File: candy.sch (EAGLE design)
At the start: 8 parts

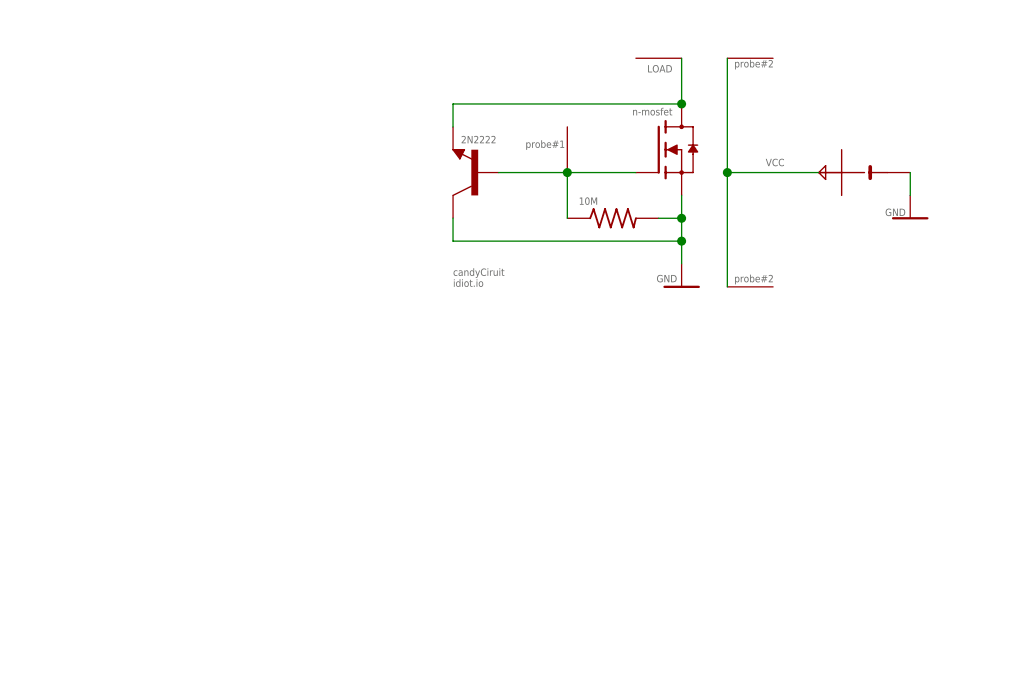
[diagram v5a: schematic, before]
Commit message: removed frame
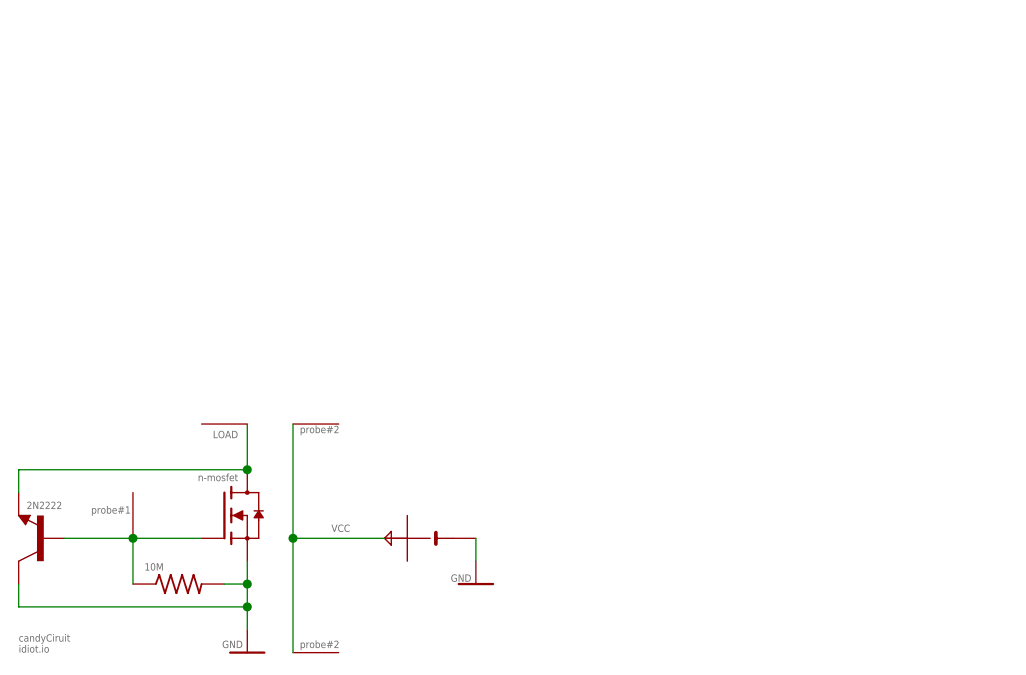
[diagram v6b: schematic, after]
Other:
- moved on the sheet: 10M, 2N2222

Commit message: stick on front
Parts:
- removed 2N2222: (no value), TinyTony_ShenzenReady:2N2222-NPN-TO92-EBC
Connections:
- net GND: no longer 2N2222.C
- net LOAD: no longer 2N2222.E
- net N$1: no longer 2N2222.B
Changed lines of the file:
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@@
 <?xml version="1.0" encoding="utf-8"?>
 <!DOCTYPE eagle SYSTEM "eagle.dtd">
-<eagle version="8.7.0">
+<eagle version="9.0.1">
 <drawing>
 <settings>
@@
 <grid distance="0.1" unitdist="inch" unit="inch" style="lines" multiple="1" display="no" altdistance="0.01" altunitdist="inch" altunit="inch"/>
 <layers>
-<layer number="1" name="Top" color="4" fill="1" visible="no" active="no"/>
-<layer number="16" name="Bottom" color="1" fill="1" visible="no" active="no"/>
-<layer number="17" name="Pads" color="2" fill="1" visible="no" active="no"/>
-<layer number="18" name="Vias" color="2" fill="1" visible="no" active="no"/>
-<layer number="19" name="Unrouted" color="6" fill="1" visible="no" active="no"/>
-<layer number="20" name="Dimension" color="24" fill="1" visible="no" active="no"/>
-<layer number="21" name="tPlace" color="7" fill="1" visible="no" active="no"/>
-<layer number="22" name="bPlace" color="7" fill="1" visible="no" active="no"/>
-<layer number="23" name="tOrigins" color="15" fill="1" visible="no" active="no"/>
-<layer number="24" name="bOrigins" color="15" fill="1" visible="no" active="no"/>
-<layer number="25" name="tNames" color="7" fill="1" visible="no" active="no"/>
-<layer number="26" name="bNames" color="7" fill="1" visible="no" active="no"/>
-<layer number="27" name="tValues" color="7" fill="1" visible="no" active="no"/>
-<layer number="28" name="bValues" color="7" fill="1" visible="no" active="no"/>
+<layer number="1" name="Top" color="4" fill="1" visible="yes" active="no"/>
+<layer number="16" name="Bottom" color="1" fill="1" visible="yes" active="no"/>
+<layer number="17" name="Pads" color="2" fill="1" visible="yes" active="no"/>
+<layer number="18" name="Vias" color="2" fill="1" visible="yes" active="no"/>
+<layer number="19" name="Unrouted" color="6" fill="1" visible="yes" active="no"/>
+<layer number="20" name="Dimension" color="24" fill="1" visible="yes" active="no"/>
+<layer number="21" name="tPlace" color="7" fill="1" visible="yes" active="no"/>
+<layer number="22" name="bPlace" color="7" fill="1" visible="yes" active="no"/>
+<layer number="23" name="tOrigins" color="15" fill="1" visible="yes" active="no"/>
+<layer number="24" name="bOrigins" color="15" fill="1" visible="yes" active="no"/>
+<layer number="25" name="tNames" color="7" fill="1" visible="yes" active="no"/>
+<layer number="26" name="bNames" color="7" fill="1" visible="yes" active="no"/>
+<layer number="27" name="tValues" color="7" fill="1" visible="yes" active="no"/>
+<layer number="28" name="bValues" color="7" fill="1" visible="yes" active="no"/>
 <layer number="29" name="tStop" color="7" fill="3" visible="no" active="no"/>
 <layer number="30" name="bStop" color="7" fill="6" visible="no" active="no"/>
@@
 <layer number="35" name="tGlue" color="7" fill="4" visible="no" active="no"/>
 <layer number="36" name="bGlue" color="7" fill="5" visible="no" active="no"/>
-<layer number="37" name="tTest" color="7" fill="1" visible="no" active="no"/>
-<layer number="38" name="bTest" color="7" fill="1" visible="no" active="no"/>
+<layer number="37" name="tTest" color="7" fill="1" visible="yes" active="no"/>
+<layer number="38" name="bTest" color="7" fill="1" visible="yes" active="no"/>
 <layer number="39" name="tKeepout" color="4" fill="11" visible="no" active="no"/>
 <layer number="40" name="bKeepout" color="1" fill="11" visible="no" active="no"/>
@@
 <layer number="44" name="Drills" color="7" fill="1" visible="no" active="no"/>
 <layer number="45" name="Holes" color="7" fill="1" visible="no" active="no"/>
-<layer number="46" name="Milling" color="3" fill="1" visible="no" active="no"/>
-<layer number="47" name="Measures" color="7" fill="1" visible="no" active="no"/>
-<layer number="48" name="Document" color="7" fill="1" visible="no" active="no"/>
-<layer number="49" name="Reference" color="7" fill="1" visible="no" active="no"/>
-<layer number="50" name="dxf" color="7" fill="1" visible="no" active="no"/>
-<layer number="51" name="tDocu" color="7" fill="1" visible="no" active="no"/>
-<layer number="52" name="bDocu" color="7" fill="1" visible="no" active="no"/>
-<layer number="53" name="tGND_GNDA" color="7" fill="1" visible="no" active="no"/>
-<layer number="54" name="bGND_GNDA" color="7" fill="1" visible="no" active="no"/>
-<layer number="56" name="wert" color="7" fill="1" visible="no" active="no"/>
-<layer number="57" name="tCAD" color="7" fill="1" visible="no" active="no"/>
-<layer number="59" name="tCarbon" color="7" fill="1" visible="no" active="no"/>
-<layer number="60" name="bCarbon" color="7" fill="1" visible="no" active="no"/>
+<layer number="46" name="Milling" color="3" fill="1" visible="yes" active="no"/>
+<layer number="47" name="Measures" color="7" fill="1" visible="yes" active="no"/>
+<layer number="48" name="Document" color="7" fill="1" visible="yes" active="no"/>
+<layer number="49" name="Reference" color="7" fill="1" visible="yes" active="no"/>
+<layer number="50" name="dxf" color="7" fill="1" visible="yes" active="no"/>
+<layer number="51" name="tDocu" color="7" fill="1" visible="yes" active="no"/>
+<layer number="52" name="bDocu" color="7" fill="1" visible="yes" active="no"/>
+<layer number="53" name="tGND_GNDA" color="7" fill="1" visible="yes" active="no"/>
+<layer number="54" name="bGND_GNDA" color="7" fill="1" visible="yes" active="no"/>
+<layer number="56" name="wert" color="7" fill="1" visible="yes" active="no"/>
+<layer number="57" name="tCAD" color="7" fill="1" visible="yes" active="no"/>
+<layer number="59" name="tCarbon" color="7" fill="1" visible="yes" active="no"/>
+<layer number="60" name="bCarbon" color="7" fill="1" visible="yes" active="no"/>
 <layer number="88" name="SimResults" color="9" fill="1" visible="yes" active="yes"/>
 <layer number="89" name="SimProbes" color="9" fill="1" visible="yes" active="yes"/>
@@
 <part name="U$5" library="TinyTony_ShenzenReady" deviceset="SMDPAD" device=""/>
 <part name="VCC" library="TinyTony_ShenzenReady" deviceset="SMDPAD" device=""/>
-<part name="U$7" library="TinyTony_ShenzenReady" library_urn="urn:adsk.eagle:library:2159173" deviceset="CR2032" device="LINX" package3d_urn="urn:adsk.eagle:package:2160680/2"/>
+<part name="U$7" library="TinyTony_ShenzenReady" library_urn="urn:adsk.eagle:library:2159173" deviceset="CR2032" device="LINX" package3d_urn="urn:adsk.eagle:package:2160680/3"/>
 <part name="GND1" library="TinyTony_ShenzenReady" deviceset="GND" device=""/>
 <part name="GND2" library="TinyTony_ShenzenReady" deviceset="GND" device=""/>
-<part name="2N2222" library="TinyTony_ShenzenReady" library_urn="urn:adsk.eagle:library:2159173" deviceset="*-NPN-" device="TO92-EBC" package3d_urn="urn:adsk.eagle:package:28763/2" technology="2N2222"/>
 </parts>
 <sheets>
@@
 <attribute name="VALUE" x="25.146" y="5.588" size="0.8128" layer="96"/>
 </instance>
-<instance part="2N2222" gate="G$1" x="5.08" y="17.78" smashed="yes" rot="R180">
-<attribute name="NAME" x="7.366" y="21.844" size="0.8128" layer="95" rot="R180"/>
-<attribute name="VALUE" x="15.24" y="12.7" size="1.778" layer="96" rot="R180"/>
-</instance>
 </instances>
 <busses>
@@
 <wire x1="15.24" y1="12.7" x2="15.24" y2="17.78" width="0.1524" layer="91"/>
 <junction x="15.24" y="17.78"/>
-<pinref part="2N2222" gate="G$1" pin="B"/>
-<wire x1="7.62" y1="17.78" x2="15.24" y2="17.78" width="0.1524" layer="91"/>
 </segment>
 </net>
@@
 <wire x1="27.94" y1="30.48" x2="27.94" y2="25.4" width="0.1524" layer="91"/>
 <label x="26.924" y="29.718" size="0.8128" layer="95" rot="R180"/>
-<wire x1="27.94" y1="25.4" x2="2.54" y2="25.4" width="0.1524" layer="91"/>
-<junction x="27.94" y="25.4"/>
-<pinref part="2N2222" gate="G$1" pin="E"/>
-<wire x1="2.54" y1="25.4" x2="2.54" y2="22.86" width="0.1524" layer="91"/>
 </segment>
 </net>
@@
 <junction x="27.94" y="12.7"/>
 <pinref part="GND2" gate="1" pin="GND"/>
-<wire x1="27.94" y1="12.7" x2="27.94" y2="10.16" width="0.1524" layer="91"/>
-<pinref part="2N2222" gate="G$1" pin="C"/>
-<wire x1="27.94" y1="10.16" x2="27.94" y2="7.62" width="0.1524" layer="91"/>
-<wire x1="2.54" y1="12.7" x2="2.54" y2="10.16" width="0.1524" layer="91"/>
-<wire x1="2.54" y1="10.16" x2="27.94" y2="10.16" width="0.1524" layer="91"/>
-<junction x="27.94" y="10.16"/>
+<wire x1="27.94" y1="12.7" x2="27.94" y2="7.62" width="0.1524" layer="91"/>
 </segment>
 </net>
